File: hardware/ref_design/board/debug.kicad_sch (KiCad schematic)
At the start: 3 parts, among them J7 DEBUG PADS, SW18 BOOT, SW19 RESET

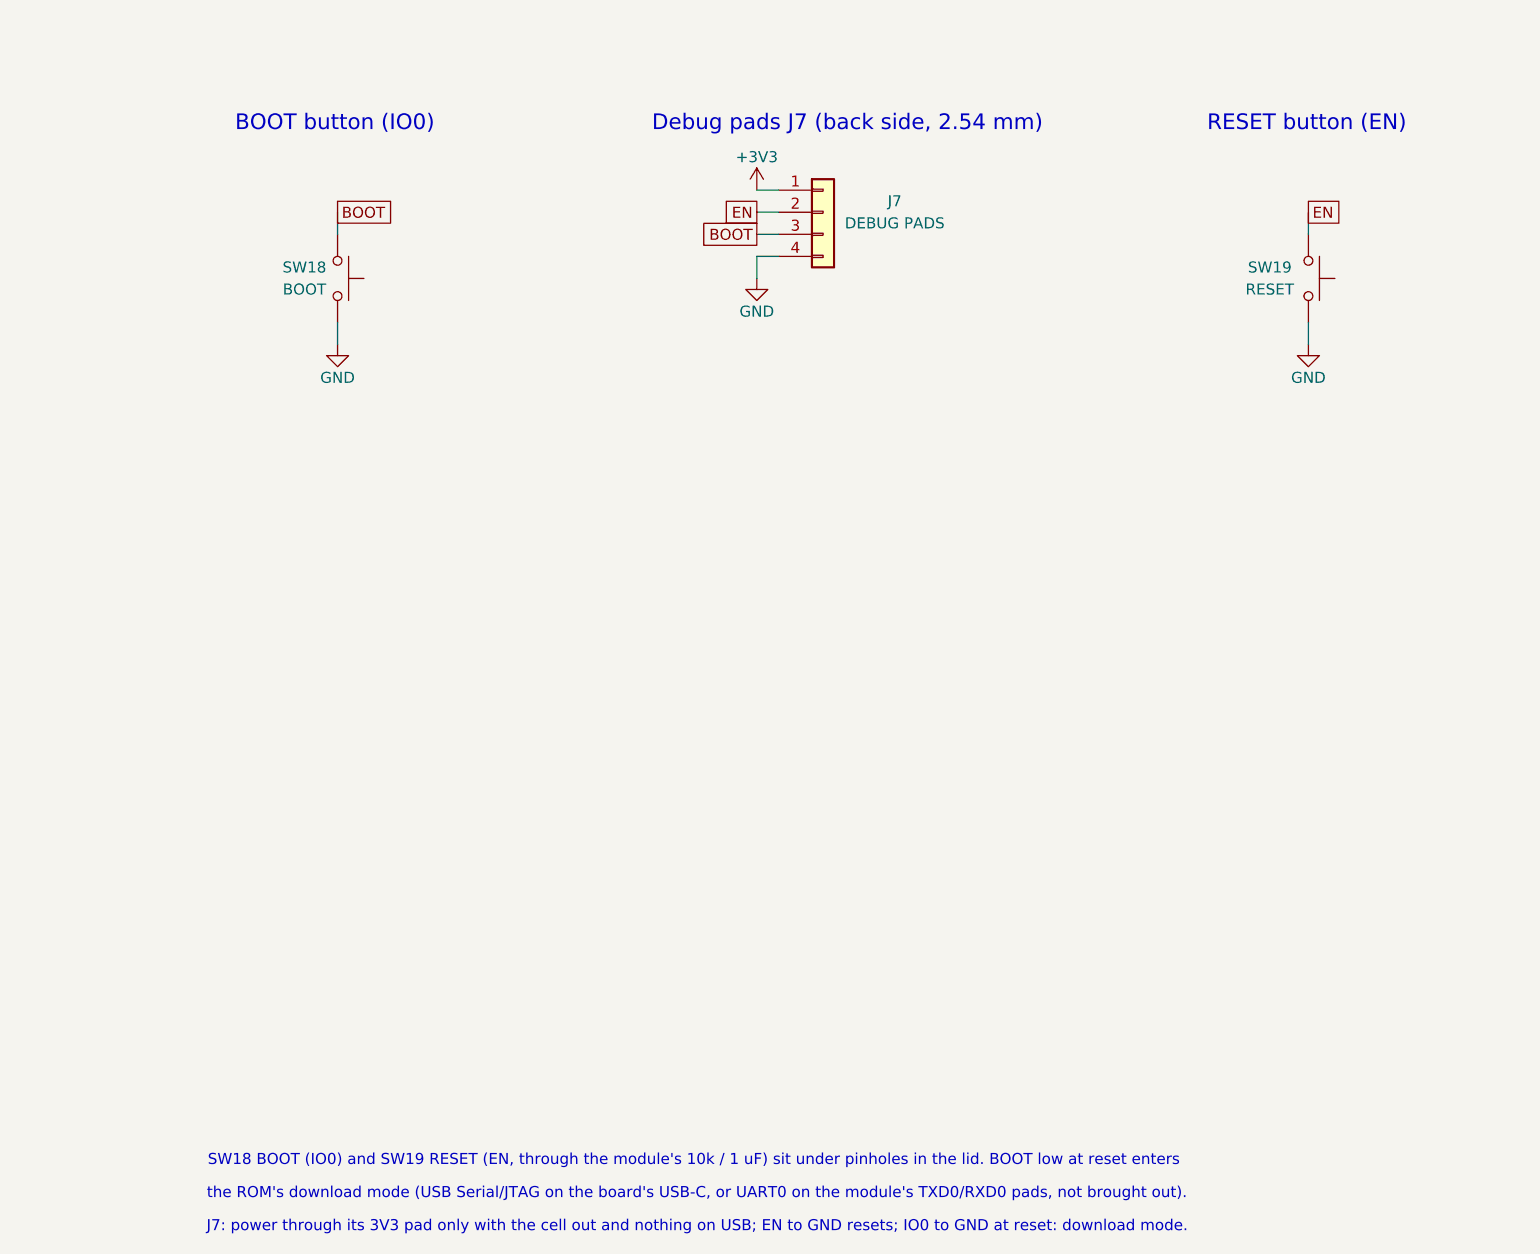
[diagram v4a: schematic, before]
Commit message: ref_design ESP32-S3: first placement (module, microSD slot with trimmed front tabs, series resistors, third register; case grow_l 1.5 for the shell tabs' copper edge), BOOT/RESET buttons dropped (J7 pads stay), place_new.py, antenna keepout, module GND vias; not routed
Co-Authored-By: Claude Sonnet 5.5 <noreply@anthropic.com>
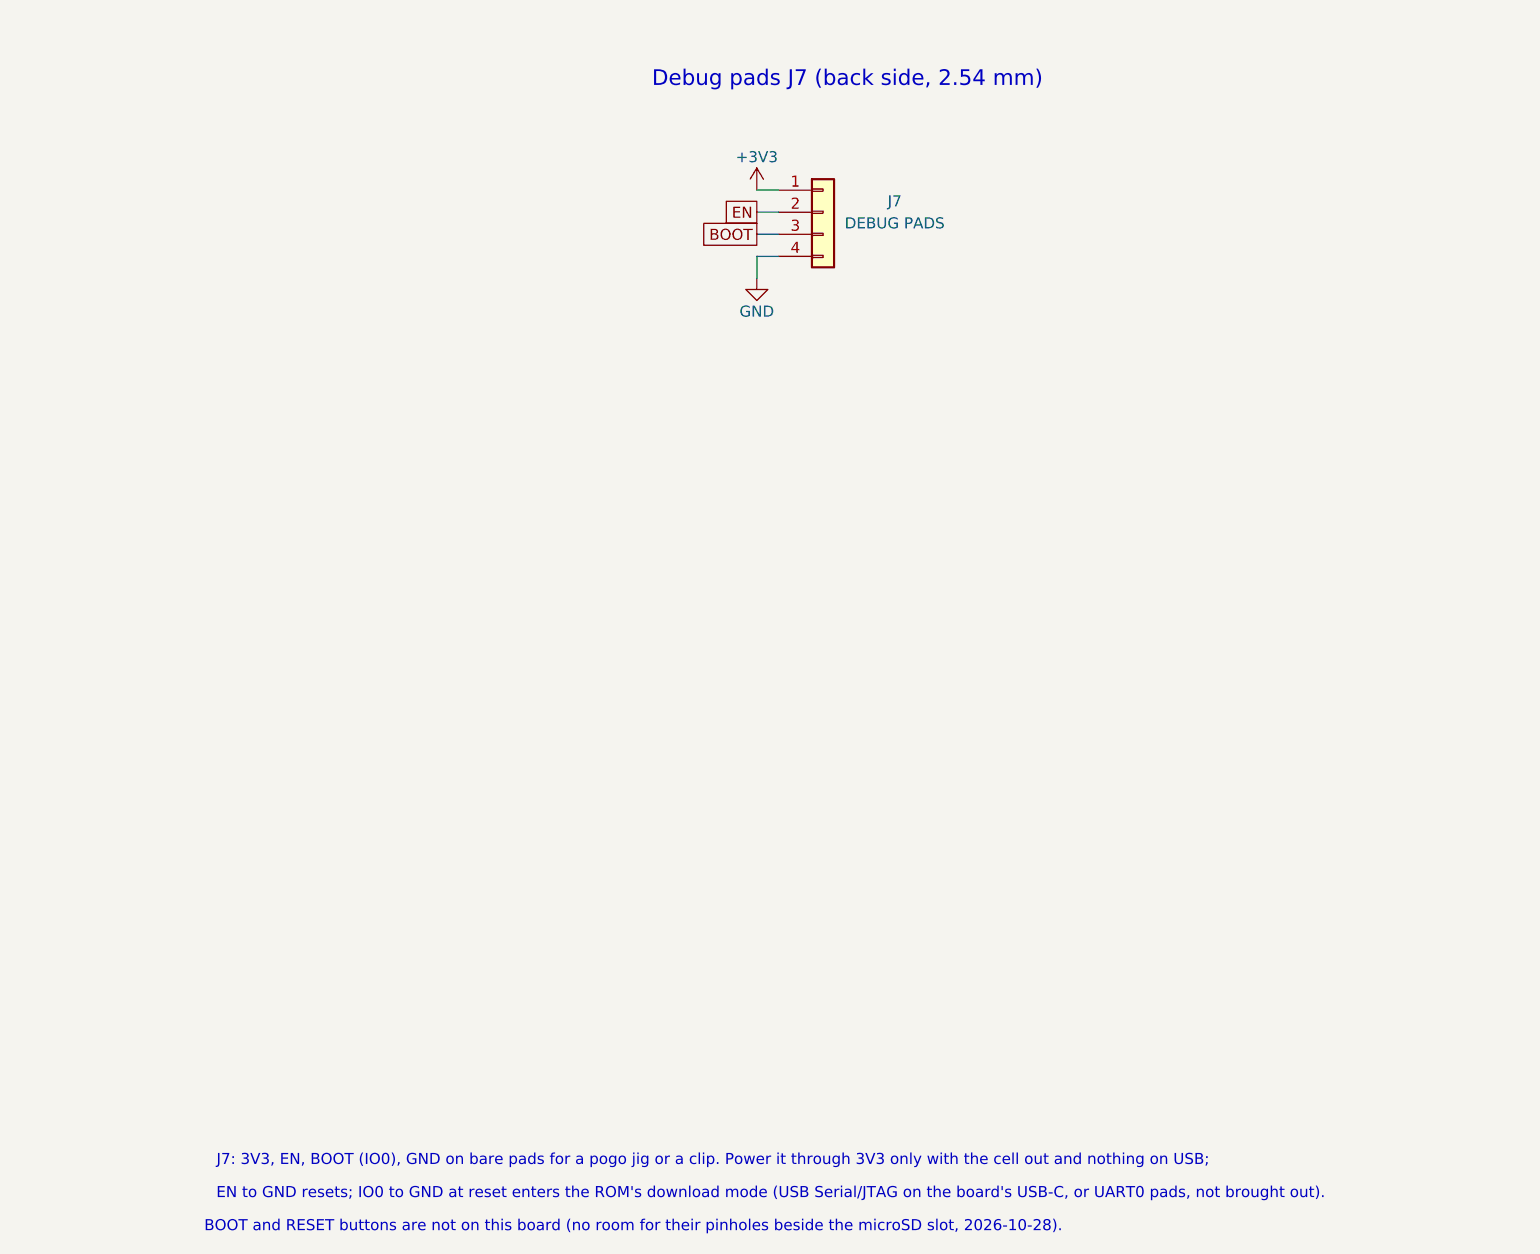
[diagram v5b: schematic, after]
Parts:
- removed SW18: BOOT, battler:SW_SPST_TS-1088-xR020, symbol Switch:SW_Push
- removed SW19: RESET, battler:SW_SPST_TS-1088-xR020, symbol Switch:SW_Push
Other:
- note added: "BOOT and RESET buttons are not on this board (no room for their pinholes beside the microSD slot, 2026-10-28)."
- note added: "EN to GND resets; IO0 to GND at reset enters the ROM's download mode (USB Serial/JTAG on the board's USB-C, or UART0 pads, not brought out)."
- note added: "J7: 3V3, EN, BOOT (IO0), GND on bare pads for a pogo jig or a clip. Power it through 3V3 only with the cell out and nothing on USB;"
- note removed: "BOOT button (IO0)"
- note removed: "J7: power through its 3V3 pad only with the cell out and nothing on USB; EN to GND resets; IO0 to GND at reset: download mode."
- note removed: "RESET button (EN)"
- note removed: "SW18 BOOT (IO0) and SW19 RESET (EN, through the module's 10k / 1 uF) sit under pinholes in the lid. BOOT low at reset enters"
- note removed: "the ROM's download mode (USB Serial/JTAG on the board's USB-C, or UART0 on the module's TXD0/RXD0 pads, not brought out)."
